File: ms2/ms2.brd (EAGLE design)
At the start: 100 x 100 mm, 156 parts, among them J1 POWERPOLE_POWER25A, J10 RS485_1, J11 I2C, J12 TTL_SERIAL, J13 Radio SPI, J14 RS485_3, J2 RAIN, J3 ADC1, J4 ON, J5 D1, J6 D2, J7 ADC2, J8 LED-EN, J9 RS485_2, Q1 DMG6602SVT, Q2 DMG6602SVT, Q3 DMG6602SVT, Q4 DMG6602SVT, Q5 DMG6602SVT, U1 LT1934ES6TRMPBF, U10 TXS0108E, U2 LT1934ES6TRMPBF, U3 DS3231SN, U4 ISL3179EIBZ, U5 ISL3179EIBZ, U6 ISL3179EIBZ, U7 TPD2E001IDRLRQ1, U8 TPS79333DBVR, U9 TPS79333DBVR, X1 67068-9000

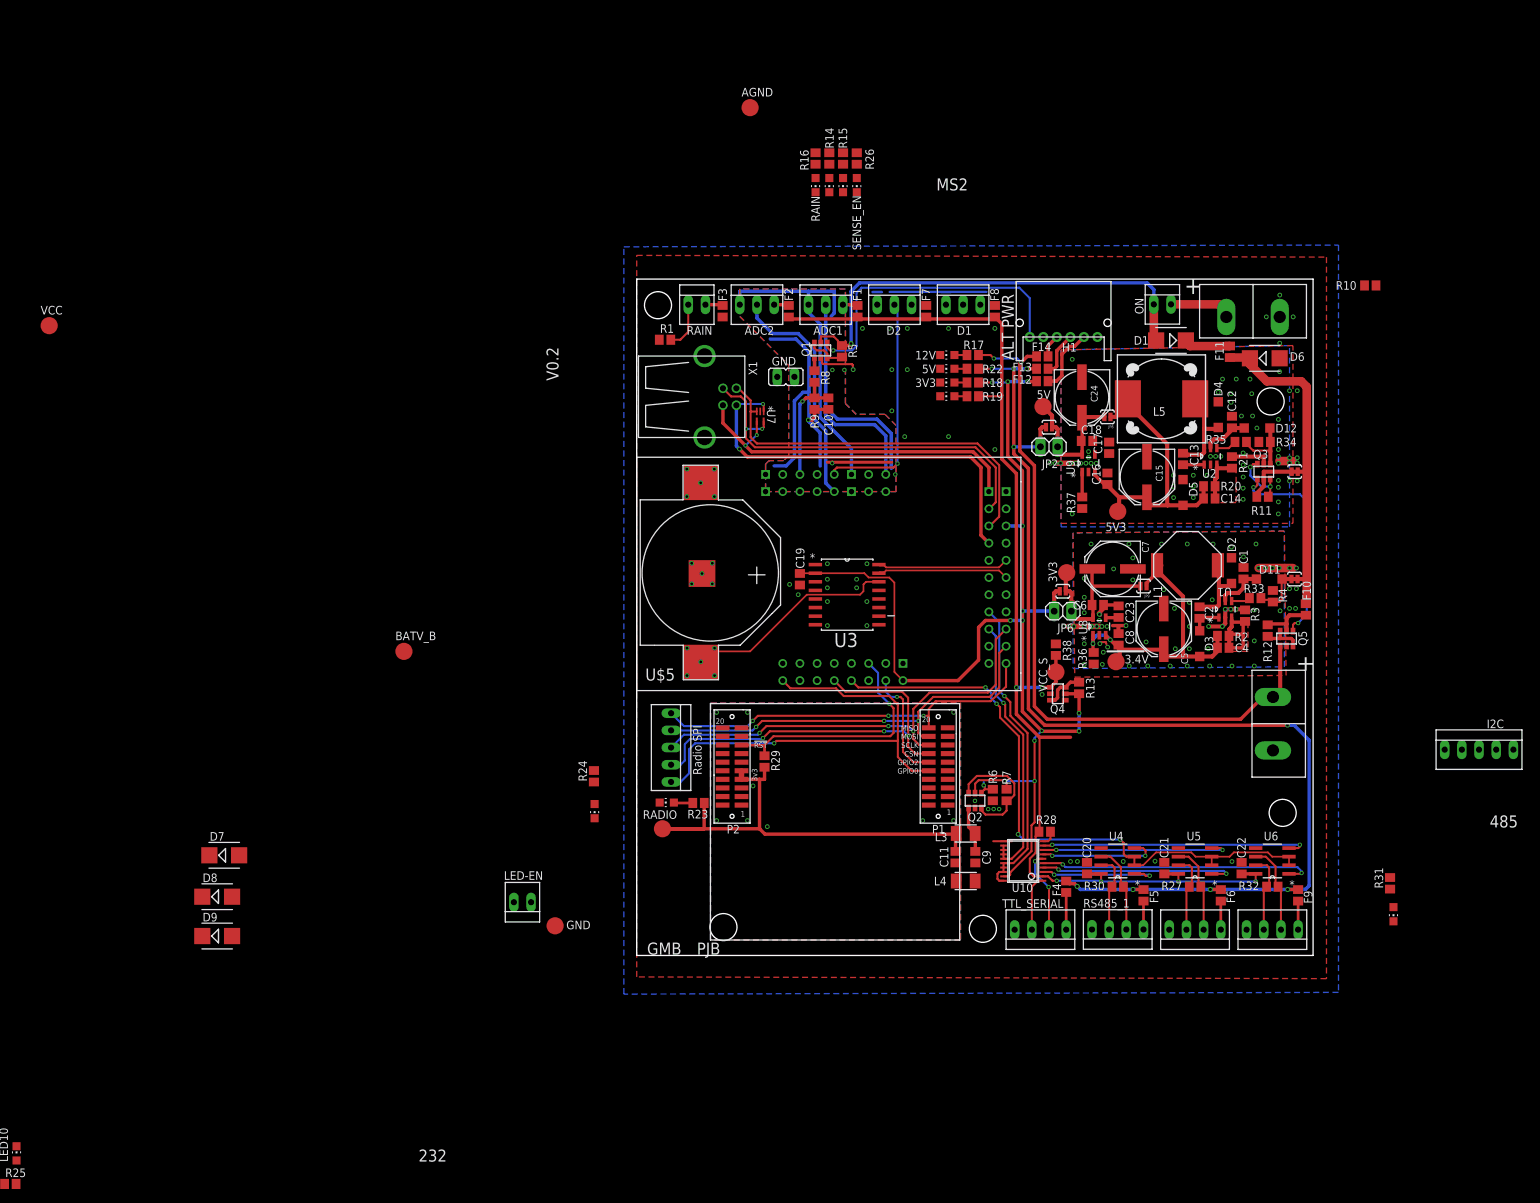
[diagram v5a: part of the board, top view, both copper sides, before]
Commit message: More MS2 layout work. 23 remaining airwires.
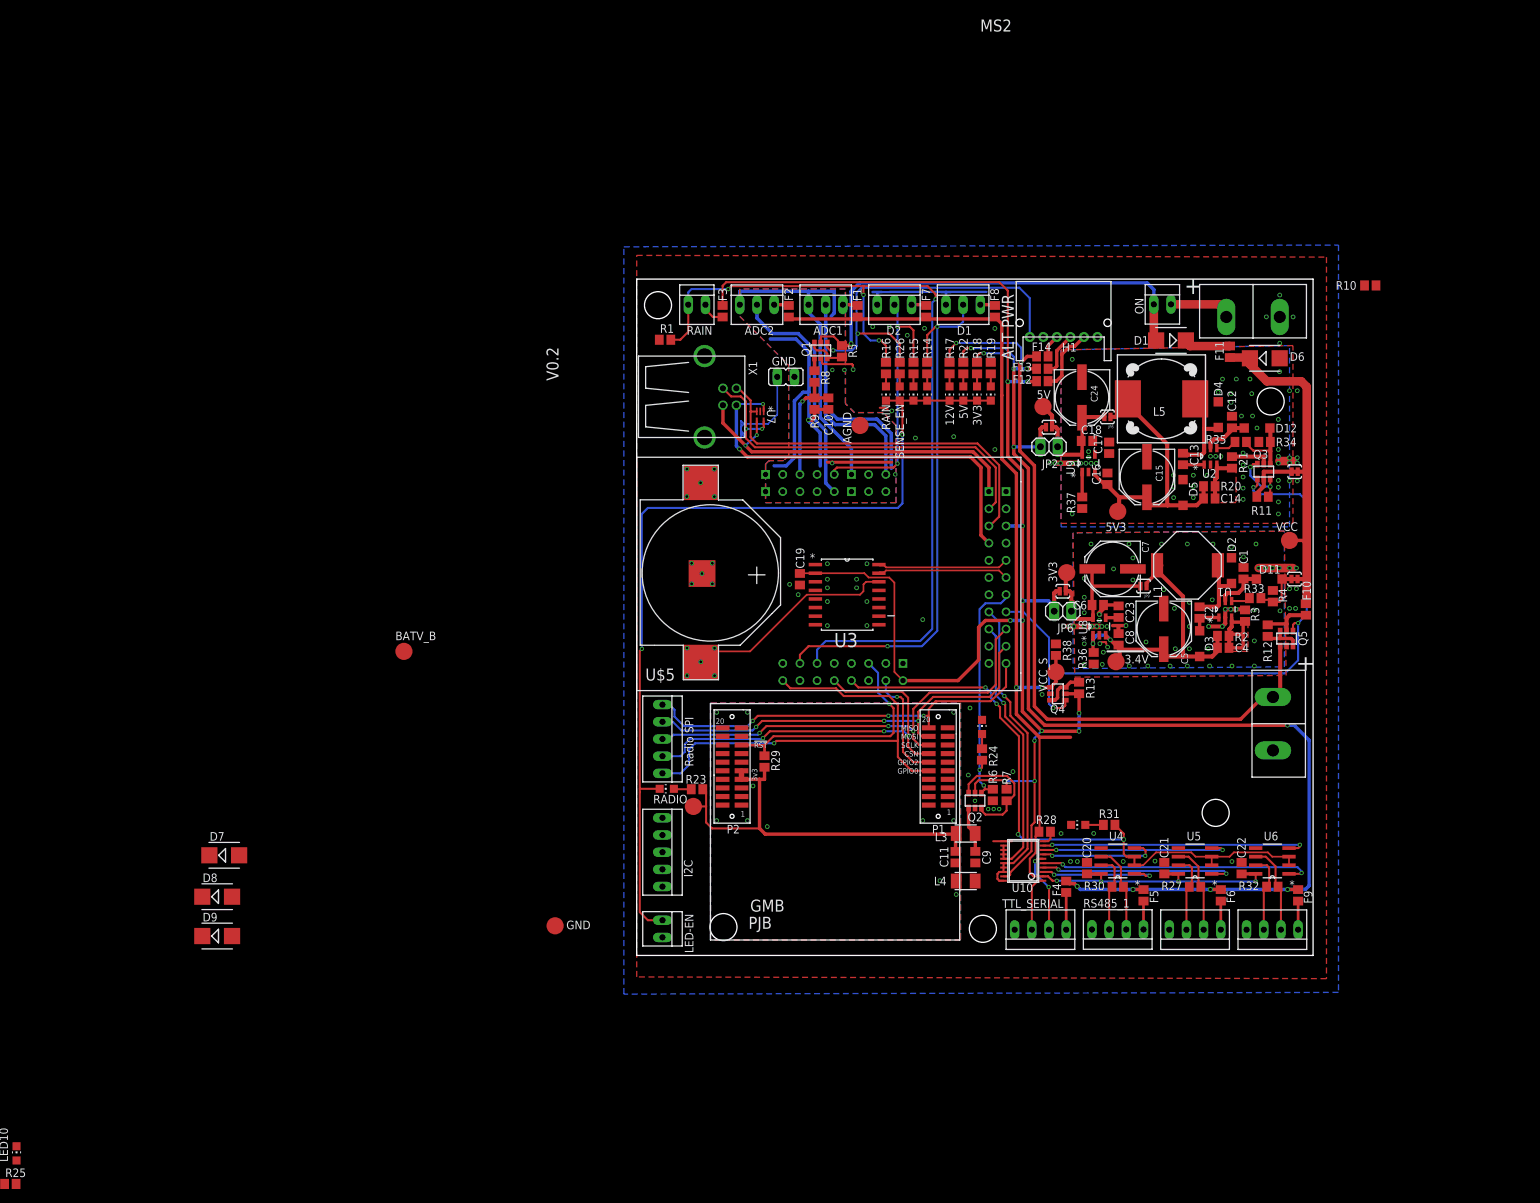
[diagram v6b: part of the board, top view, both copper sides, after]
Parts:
- moved VCC 186.1 mm to (96.5, 61.4)
- moved J11 123.1 mm to (3.68, 14.1), turned to 90 degrees
- moved LED9 58.6 mm to (51.1, 33.8), turned to 0 degrees
- moved R24 57.5 mm to (51.1, 29.7), turned to 270 degrees
- moved AGND 49.7 mm to (33.0, 78.4)
- moved LED12 48.4 mm to (65.3, 19.3), turned to 90 degrees
- moved R31 42.4 mm to (69.8, 19.3), turned to 0 degrees
- moved R14 34.2 mm to (43.0, 86.8)
- moved LED1 34.0 mm to (43.0, 83.1)
- moved R15 32.7 mm to (40.9, 86.8)
- moved R16 32.7 mm to (36.9, 86.8)
- moved LED2 32.5 mm to (40.9, 83.1)
- moved LED3 32.5 mm to (36.9, 83.1)
- moved R26 31.6 mm to (38.9, 86.8)
- moved LED11 31.5 mm to (38.9, 83.1)
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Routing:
- net LGND: track 0.00 -> 135.6 mm, vias 0 -> 2
- net RAIN: track 7.08 -> 129.9 mm, vias 0 -> 4
- net DIO_1: track 0.00 -> 80.7 mm, vias 0 -> 2
- net SENSE_EN: track 76.6 -> 150.8 mm, vias 3 -> 5
- net +3V3: track 176.3 -> 241.9 mm
- net RADIO_EN: track 3.78 -> 36.3 mm, vias 1 -> 2
- net GND: track 63.8 -> 87.1 mm, vias 163 -> 167
- net RADIO_3V3: track 75.8 -> 61.1 mm
- net SENSE_12V: track 106.6 -> 115.2 mm
- net DIO_2: track 34.1 -> 41.4 mm, vias 1 -> 2
- net SENSE_5V: track 173.6 -> 179.9 mm
- net SENSE_3V3: track 179.0 -> 175.7 mm
- net TX_EN: track 91.8 -> 94.8 mm
- net N$27: track 0.00 -> 2.67 mm
- net +12V: track 66.8 -> 69.4 mm
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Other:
- board text removed: "232"
- board text removed: "485"

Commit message: MS2 as submitted for manufacture
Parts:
- removed BATV_B: 5V B, testpad:B2,54
- removed D6, D7, D8, D9: (no value), diode:SMB
- removed F12: 250mA, farnell-parts:0805
- removed F13, F14: MCF0805, farnell-parts:0805
- added F15, F16: MCF0805, farnell-parts:0805
- added JP1: SENSE_EN, pinhead:1X02
- added JP11: RADIO_EN, pinhead:1X02
- added JP12: (no value), SparkFun-Passives:SJ_2S-NO
- added R39: 100K, resistor:R0805
- added U11: SN74HC21PW, CC11x:SOP65P640X120-14N
- 12V_OUT, J1: value POWERPOLE_POWER25A -> POWERPOLE_POWER45A; device powerpoles:POWERPOLE_PAIR_25A -> powerpoles:POWERPOLE_PAIR_45A
- LED10: value RADIO_EN -> VCC
- R25: value 56 -> 560
- R28: value 47K -> 100K
- R38: value 1M -> 100K
- moved R25 174.9 mm to (34.0, 86.8), turned to 90 degrees
- moved LED10 168.6 mm to (34.0, 83.1), turned to 180 degrees
- moved GND 94.2 mm to (62.5, 62.0)
- moved R10 75.3 mm to (48.8, 53.1), turned to 270 degrees
- moved R38 28.2 mm to (54.4, 18.0)
- moved LED12 16.4 mm to (81.5, 21.1), turned to 270 degrees
- moved U10 8.30 mm to (60.5, 21.6)
- moved R28 8.01 mm to (52.3, 18.0), turned to 90 degrees
- moved R31 7.08 mm to (76.7, 21.1), turned to 180 degrees
- moved C16 3.87 mm to (68.1, 66.9), turned to 270 degrees
- moved AGND 1.02 mm to (32.0, 78.4)
- moved F4 0.80 mm to (64.2, 9.86)
- moved F11 0.51 mm to (88.2, 89.3)
- moved 12V_OUT 0.51 mm to (94.9, 33.8)
- moved LED9 0.25 mm to (50.8, 33.8)
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- renumbered U$5 to Z1, VCC to 12V
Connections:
- removed net ALT_3V3: F12.1, H1.2
- removed net ALT_5V: F13.1, H1.3
- removed net ALT_9V: F14.1, H1.4
- new net N$47: F16.1, J11.4
- new net N$50: F15.1, J11.5
- new net N$53: LED10.A, R25.1
- new net N$57: U10.17
- new net N$58: U10.16
- new net TX_EN_BUFF: U10.3, U4.2, U4.3, U5.2, U5.3, U6.2, U6.3
- new net UART1_RX_BUFF: JP12.2, U10.1, U11.8
- net +12V: no longer D6.C
- net +3V3: now also H1.2, JP1.1, JP11.1; no longer F12.2
- net 485_RX_1: now also JP12.1, U11.10; no longer U10.3
- net 485_RX_2: now also R28.1, U11.12; no longer U10.4
- net 485_RX_3: now also R38.1, U11.13; no longer U10.5
- net GND: now also U11.1, U11.2, U11.4, U11.5, U11.7, Z1.B18; no longer D6.A, R38.2
- net LGND: now also LED10.C
- net N$8: now also U11.6; no longer R28.1, U10.10
- net RADIO_EN: now also JP11.2
- net SENSE_12V: now also H1.4; no longer F14.2
- net SENSE_3V3: now also F16.2, R38.2, R39.2, U10.4, U10.5, U11.14; no longer J11.4, R38.1
- net SENSE_5V: now also F15.2, H1.3; no longer F13.2, J11.5
- net SENSE_EN: now also JP1.2, U10.10
- net TTL_RX: now also R39.1, U11.9; no longer U10.1
- net TX_EN: now also U10.18; no longer U4.2, U4.3, U5.2, U5.3, U6.2, U6.3
- net UART1_RX: no longer U10.16, U10.17, U10.18
- net VBAT_B: no longer BATV_B.TP
- net VCC: now also R25.2
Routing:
- net LGND: track 135.6 -> 252.9 mm, vias 2 -> 5
- net SENSE_EN: track 150.8 -> 252.7 mm, vias 5 -> 7
- net I2C_SDA: track 19.4 -> 95.7 mm, vias 0 -> 1
- net I2C_SCL: track 19.4 -> 92.6 mm, vias 0 -> 1
- net SENSE_5V: track 179.9 -> 253.1 mm, vias 9 -> 10
- net SENSE_3V3: track 175.7 -> 244.6 mm, vias 6 -> 7
- net GND: track 87.1 -> 142.6 mm, vias 167 -> 358
- net TX_EN_BUFF: track 0.00 -> 44.6 mm
- net TX_EN: track 94.8 -> 61.9 mm, vias 4 -> 5
- net UART1_RX_BUFF: track 0.00 -> 11.8 mm, vias 0 -> 2
- net 485_RX_2: track 29.7 -> 40.7 mm, vias 2 -> 4
- net ALT_3V3: track 9.86 -> 0.00 mm
- net UART1_TX: track 39.9 -> 30.7 mm
- net +3V3: track 241.9 -> 251.0 mm, vias 13 -> 12
- net UART1_RX: track 45.9 -> 37.3 mm
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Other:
- board text added: "ADC1_IN ADC1_PWR ADC2_IN ADC2_PWR RTC"
- board text added: "ASSEMBLY DATE"
- board text added: "Graeme Bragg Kirk Martinez Phil Basford ECS University of Southampton"
- board text added: "MS2 V1.0"
- board text added: "RADIO_EN RADIO_3V3 CC1120"
- board text added: "RAIN D1 D2 BATVOLTS BATVOLTS_DIV"
- board text added: "TTL_S RS485_1 RS485_2 RS485_3"
- board text added: "VCC 3V3 SENSE_EN SENSE_3V3 SENSE_5V SENSE_12V"
- board text added: "mountainsensing.org"
- board text removed: "GMB"
- board text removed: "MS2"
- board text removed: "PJB"
- board text removed: "V0.2"
